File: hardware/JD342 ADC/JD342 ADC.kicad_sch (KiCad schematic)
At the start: 12 parts, among them U1 ADS7279IPW, U2 OPA192IDBVR

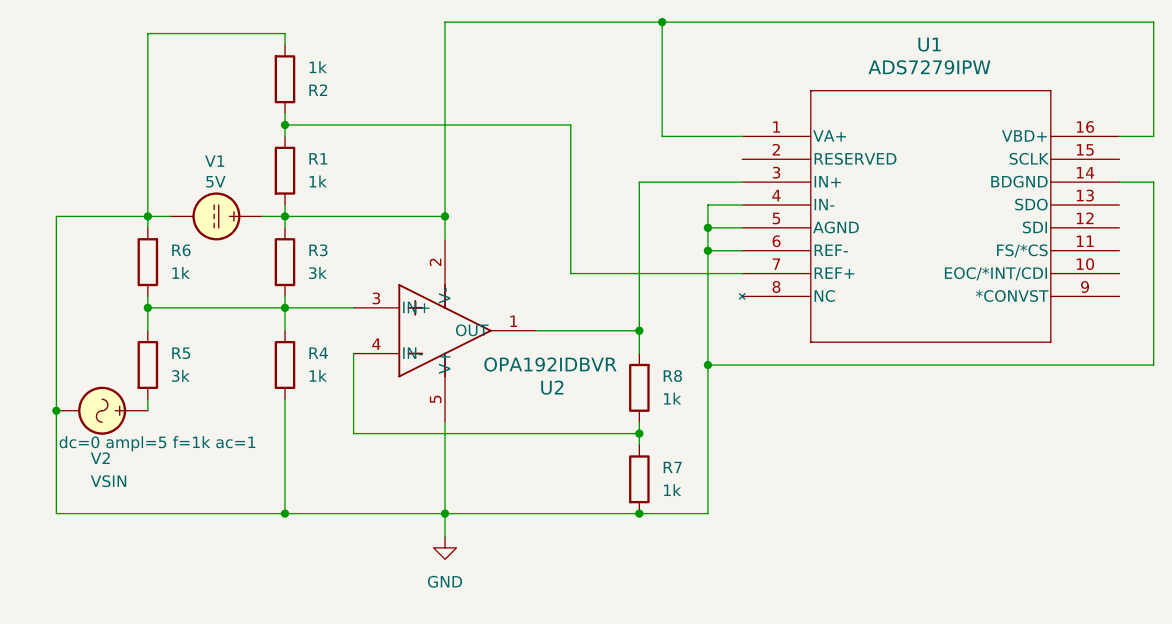
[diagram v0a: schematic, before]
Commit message: feat: small tweaks to adc schematic structure
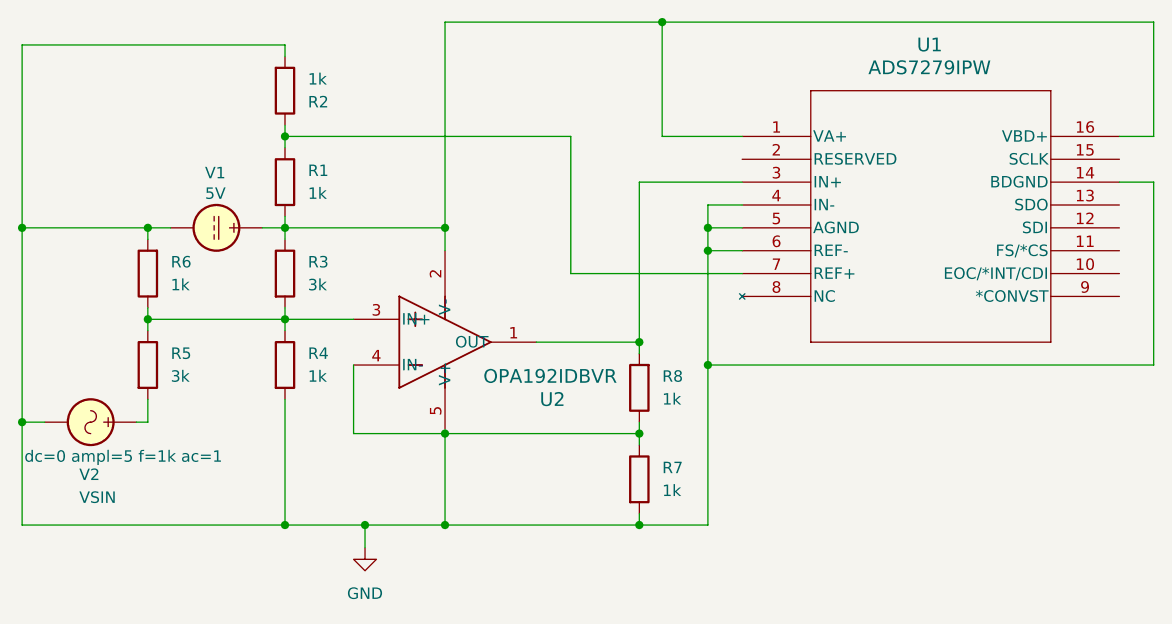
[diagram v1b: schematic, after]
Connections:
- net GND: now also R7.1, R8.1, U2.4 (IN-)
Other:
- moved on the sheet: R1, R2, R3, R6, U2, V1, V2
